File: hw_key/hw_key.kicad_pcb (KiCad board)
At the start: 2 copper layers, 127 x 38.1 mm, 30 parts, among them P2 CONN_01X10, SW1 SW_PUSH_SMALL_H, SW10 SW_PUSH_SMALL_H, SW11 SW_PUSH_SMALL_H, SW12 SW_PUSH_SMALL_H, SW2 SW_PUSH_SMALL_H, SW3 SW_PUSH_SMALL_H, SW4 SW_PUSH_SMALL_H, SW5 SW_PUSH_SMALL_H, SW6 SW_PUSH_SMALL_H, SW7 SW_PUSH_SMALL_H, SW8 SW_PUSH_SMALL_H, SW9 SW_PUSH_SMALL_H

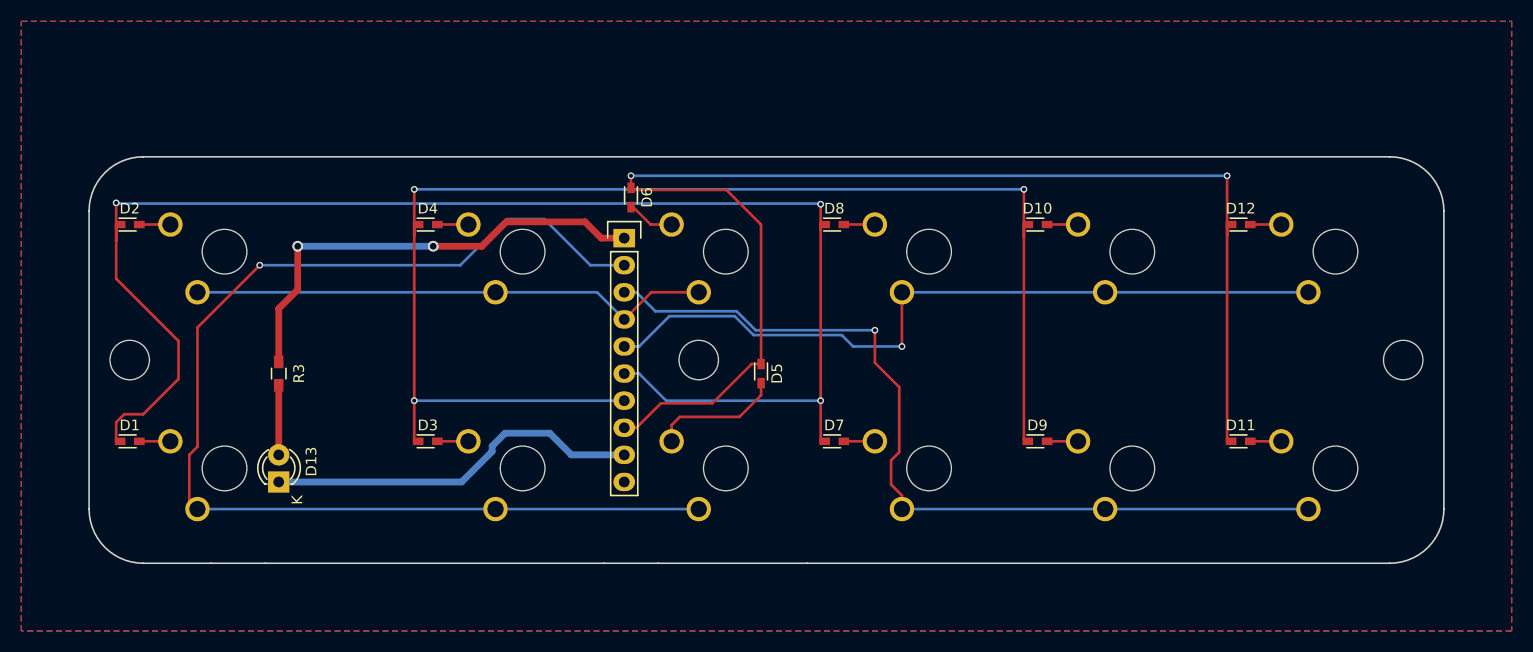
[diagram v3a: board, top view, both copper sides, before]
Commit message: hole position, corner rounding size
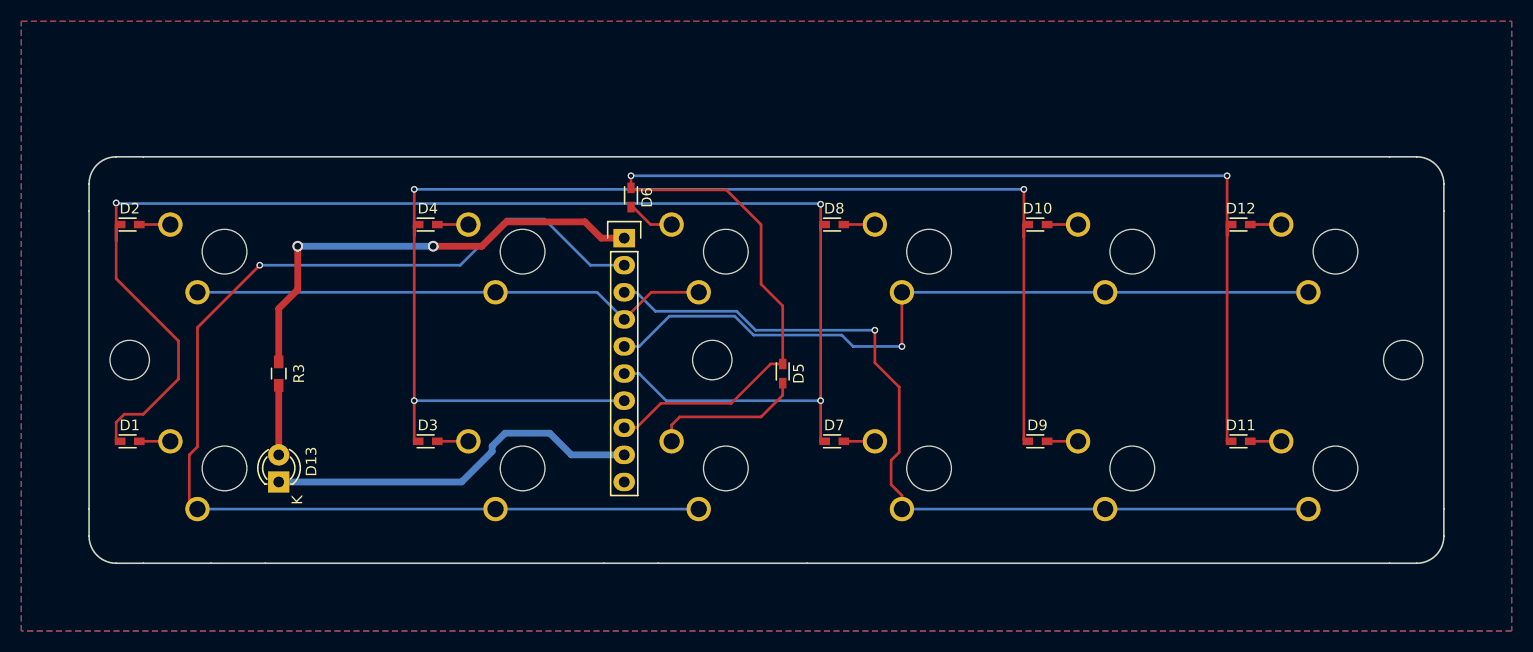
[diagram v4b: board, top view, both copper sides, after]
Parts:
- moved D5 2.03 mm to (90.4, 45.7)
- moved REF** 1.27 mm to (83.8, 44.5)
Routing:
- net /kR2: track 125.8 -> 128.6 mm
- net Net-(D5-Pad2): track 12.2 -> 14.2 mm
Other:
- outline, holes or cut-outs redrawn
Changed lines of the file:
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@@
     (area 19.05 12.7 158.750001 69.850001)
     (thickness 1.6)
-    (drawings 14)
-    (tracks 144)
+    (drawings 22)
+    (tracks 146)
     (zones 0)
     (modules 30)
@@
     (mod_text_size 1 1)
     (mod_text_width 0.15)
-    (pad_size 1.5 1.5)
-    (pad_drill 0.8)
+    (pad_size 3.7 3.7)
+    (pad_drill 3.7)
     (pad_to_mask_clearance 0.2)
     (aux_axis_origin 0 0)
@@
   )
   (module Mounting_Holes:MountingHole_3.7mm (layer F.Cu)
-    (at 82.55 44.45)
+    (at 83.82 44.45)
     (descr "Mounting Hole 3.7mm, no annular")
     (tags "mounting hole 3.7mm no annular")
@@
   )
   (module components:SOD-523-handsoldering (layer F.Cu)
-    (at 88.392 45.72 270)
+    (at 90.424 45.72 270)
     (descr "http://www.diodes.com/datasheets/ap02001.pdf p.144")
     (tags "Diode SOD523")
@@
     (pad 1 np_thru_hole circle (at 0 0) (size 3.7 3.7) (drill 3.7) (layers *.Cu *.Mask))
   )
+  (gr_line (start 25.4 60.96) (end 25.4 58.42) (angle 90) (layer Edge.Cuts) (width 0.15))
+  (gr_line (start 27.94 63.5) (end 30.48 63.5) (angle 90) (layer Edge.Cuts) (width 0.15))
+  (gr_line (start 25.4 27.94) (end 25.4 30.48) (angle 90) (layer Edge.Cuts) (width 0.15))
+  (gr_line (start 30.48 25.4) (end 27.94 25.4) (angle 90) (layer Edge.Cuts) (width 0.15))
+  (gr_line (start 149.86 63.5) (end 147.32 63.5) (angle 90) (layer Edge.Cuts) (width 0.15))
+  (gr_line (start 152.4 60.96) (end 152.4 58.42) (angle 90) (layer Edge.Cuts) (width 0.15))
+  (gr_line (start 152.4 27.94) (end 152.4 30.48) (angle 90) (layer Edge.Cuts) (width 0.15))
+  (gr_line (start 149.86 25.4) (end 147.32 25.4) (angle 90) (layer Edge.Cuts) (width 0.15))
+  (gr_arc (start 149.86 27.94) (end 149.86 25.4) (angle 90) (layer Edge.Cuts) (width 0.15))
+  (gr_arc (start 149.86 60.96) (end 152.4 60.96) (angle 90) (layer Edge.Cuts) (width 0.15))
+  (gr_arc (start 27.94 60.96) (end 27.94 63.5) (angle 90) (layer Edge.Cuts) (width 0.15))
+  (gr_arc (start 27.94 27.94) (end 25.4 27.94) (angle 90) (layer Edge.Cuts) (width 0.15))
   (gr_line (start 36.83 63.5) (end 41.91 63.5) (angle 90) (layer Edge.Cuts) (width 0.15))
   (gr_line (start 78.74 63.5) (end 73.66 63.5) (angle 90) (layer Edge.Cuts) (width 0.15))
@@
   (gr_line (start 25.4 30.48) (end 25.4 58.42) (angle 90) (layer Edge.Cuts) (width 0.15))
   (gr_line (start 147.32 25.4) (end 30.48 25.4) (angle 90) (layer Edge.Cuts) (width 0.15))
-  (gr_arc (start 147.32 30.48) (end 147.32 25.4) (angle 90) (layer Edge.Cuts) (width 0.15))
-  (gr_arc (start 147.32 58.42) (end 152.4 58.42) (angle 90) (layer Edge.Cuts) (width 0.15))
-  (gr_arc (start 30.48 58.42) (end 30.48 63.5) (angle 90) (layer Edge.Cuts) (width 0.15))
-  (gr_arc (start 30.48 30.48) (end 25.4 30.48) (angle 90) (layer Edge.Cuts) (width 0.15))
   (target plus (at 25.4 25.4) (size 5) (width 0.15) (layer Edge.Cuts))
   (segment (start 30.11 52.07) (end 33.02 52.07) (width 0.254) (layer F.Cu) (net 1) (status 30))
@@
   (segment (start 60.96 52.07) (end 58.05 52.07) (width 0.254) (layer F.Cu) (net 3) (status 30))
   (segment (start 60.96 31.75) (end 58.05 31.75) (width 0.254) (layer F.Cu) (net 4) (status 30))
-  (segment (start 88.392 46.62) (end 88.392 47.752) (width 0.254) (layer F.Cu) (net 5) (status 10))
+  (segment (start 90.424 46.62) (end 90.424 47.752) (width 0.254) (layer F.Cu) (net 5) (status 10))
+  (segment (start 88.392 49.784) (end 80.772 49.784) (width 0.254) (layer F.Cu) (net 5))
+  (segment (start 80.772 49.784) (end 80.01 50.546) (width 0.254) (layer F.Cu) (net 5))
   (segment (start 80.01 50.546) (end 80.01 52.07) (width 0.254) (layer F.Cu) (net 5) (status 20))
-  (segment (start 80.772 49.784) (end 80.01 50.546) (width 0.254) (layer F.Cu) (net 5))
-  (segment (start 86.36 49.784) (end 80.772 49.784) (width 0.254) (layer F.Cu) (net 5))
-  (segment (start 88.392 47.752) (end 86.36 49.784) (width 0.254) (layer F.Cu) (net 5))
+  (segment (start 90.424 47.752) (end 88.392 49.784) (width 0.254) (layer F.Cu) (net 5))
   (segment (start 80.01 31.75) (end 78.04 31.75) (width 0.254) (layer F.Cu) (net 6) (status 10))
   (segment (start 78.04 31.75) (end 76.2 29.91) (width 0.254) (layer F.Cu) (net 6) (status 20))
@@
   (segment (start 113.157 52.07) (end 113.4 52.07) (width 0.254) (layer F.Cu) (net 16) (status 30))
   (segment (start 55.88 48.26) (end 55.88 32.766) (width 0.254) (layer F.Cu) (net 16))
-  (segment (start 88.392 44.82) (end 87.514 44.82) (width 0.254) (layer F.Cu) (net 17) (status 10))
+  (segment (start 78.994 48.514) (end 85.598 48.514) (width 0.254) (layer F.Cu) (net 17))
+  (segment (start 89.292 44.82) (end 90.424 44.82) (width 0.254) (layer F.Cu) (net 17) (status 20))
+  (segment (start 85.598 48.514) (end 89.292 44.82) (width 0.254) (layer F.Cu) (net 17))
+  (segment (start 90.424 44.82) (end 90.424 39.37) (width 0.254) (layer F.Cu) (net 17) (status 10))
+  (segment (start 88.392 31.75) (end 85.152 28.51) (width 0.254) (layer F.Cu) (net 17))
+  (segment (start 85.152 28.51) (end 76.2 28.51) (width 0.254) (layer F.Cu) (net 17) (status 20))
+  (segment (start 88.392 31.75) (end 88.392 37.338) (width 0.254) (layer F.Cu) (net 17))
+  (segment (start 90.424 39.37) (end 88.392 37.338) (width 0.254) (layer F.Cu) (net 17))
   (segment (start 76.708 50.8) (end 75.565 50.8) (width 0.254) (layer F.Cu) (net 17) (status 20))
   (segment (start 78.994 48.514) (end 76.708 50.8) (width 0.254) (layer F.Cu) (net 17))
-  (segment (start 83.82 48.514) (end 78.994 48.514) (width 0.254) (layer F.Cu) (net 17))
-  (segment (start 87.514 44.82) (end 83.82 48.514) (width 0.254) (layer F.Cu) (net 17))
-  (segment (start 88.392 31.75) (end 88.392 44.82) (width 0.254) (layer F.Cu) (net 17) (status 20))
   (segment (start 132.08 52.07) (end 132.08 32.766) (width 0.254) (layer F.Cu) (net 17) (status 10))
   (segment (start 132.08 52.07) (end 132.45 52.07) (width 0.254) (layer F.Cu) (net 17) (status 30))
@@
   (segment (start 76.2 28.51) (end 76.2 27.178) (width 0.254) (layer F.Cu) (net 17) (status 10))
   (via (at 132.08 27.178) (size 0.635) (drill 0.381) (layers F.Cu B.Cu) (net 17))
-  (segment (start 85.152 28.51) (end 76.2 28.51) (width 0.254) (layer F.Cu) (net 17) (status 20))
-  (segment (start 88.392 31.75) (end 85.152 28.51) (width 0.254) (layer F.Cu) (net 17))
   (segment (start 68.58 51.308) (end 64.389 51.308) (width 0.635) (layer B.Cu) (net 18))
   (segment (start 70.612 53.34) (end 68.58 51.308) (width 0.635) (layer B.Cu) (net 18))

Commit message: revamp boards (for assembled height)
flip logic over so that it can mate closely with key; reset button moves
to same side as all the other parts; board assembly down to ~16mm high
and assembly more easily lends itself to angling for even less height at
the front for slightly more in the back
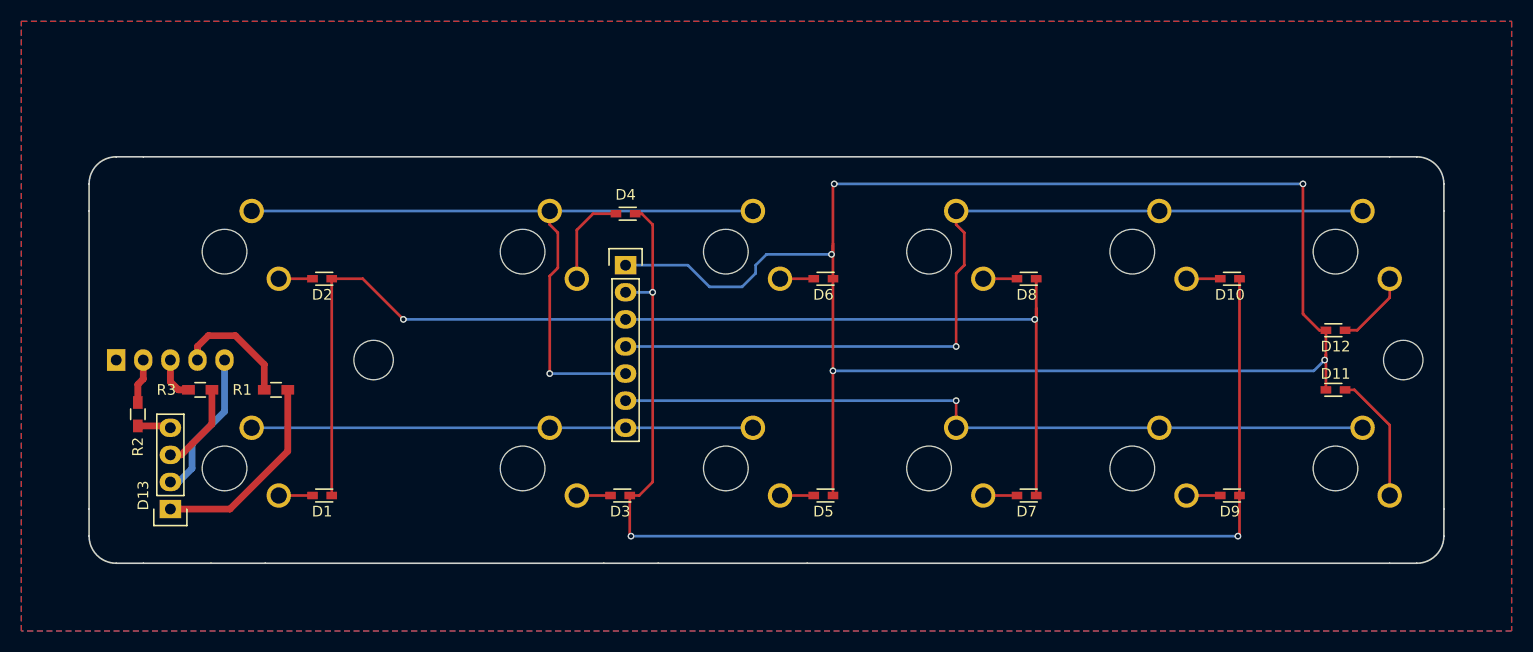
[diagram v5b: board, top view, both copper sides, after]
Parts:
- removed the REF** at (29.2, 44.5)
- added P1: CONN_01X07, Pin_Headers:Pin_Header_Straight_1x07, F.Cu at (75.7, 35.6)
- added R1: 330, Resistors_SMD:R_0603_HandSoldering, F.Cu at (42.9, 47.2)
- added R2: 330, Resistors_SMD:R_0603_HandSoldering, F.Cu at (30.0, 49.5)
- D13: value LED -> LED_RABG; footprint LEDs:LED-3MM -> Pin_Headers:Pin_Header_Straight_1x04
- P2: value CONN_01X10 -> CONN_01X05; footprint Pin_Headers:Pin_Header_Straight_1x10 -> Pin_Headers:Pin_Header_Straight_1x05; moved to B.Cu
- moved P2 49.0 mm to (27.9, 44.5), turned to 270 degrees
- moved REF** 31.7 mm to (52.1, 44.5)
- moved D6 19.6 mm to (94.2, 36.8), turned to 180 degrees
- moved D10 18.7 mm to (132.3, 36.8), turned to 180 degrees
- moved D7 18.7 mm to (113.3, 57.1), turned to 180 degrees
- moved D8 18.7 mm to (113.3, 36.8), turned to 180 degrees
- moved D9 18.7 mm to (132.3, 57.1), turned to 180 degrees
- moved D1 18.7 mm to (47.2, 57.1), turned to 180 degrees
- moved D2 18.7 mm to (47.2, 36.8), turned to 180 degrees
- moved D3 18.7 mm to (75.2, 57.1), turned to 180 degrees
- moved D4 18.6 mm to (75.7, 30.7), turned to 180 degrees
- moved D12 13.3 mm to (142.2, 41.7)
- moved D5 12.0 mm to (94.2, 57.1), turned to 180 degrees
- moved D13 10.5 mm to (33.0, 58.4), turned to 180 degrees
- moved D11 10.1 mm to (142.2, 47.2)
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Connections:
- D13 pad 1: /kLED_MACRO -> Net-(D13-Pad1)
- D13 pad 2: Net-(D13-Pad2) -> +3V3
- P2 pad 1: +3V3 -> GND
- P2 pad 2: /kC0 -> /LED_B
- P2 pad 3: /kC1 -> /LED_G
- P2 pad 4: /kC2 -> /LED_R
- P2 pad 5: /kC3 -> +3V3
- R3 pad 1: +3V3 -> Net-(D13-Pad3)
- R3 pad 2: Net-(D13-Pad2) -> /LED_G
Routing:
- net /kC0: track 110.6 -> 47.0 mm, vias 1 -> 0
- net /kLED_MACRO: track 35.4 -> 0.00 mm
- net /kR2: track 128.6 -> 163.6 mm, vias 2 -> 5
- net /kR0: track 140.1 -> 109.3 mm, vias 3 -> 2
- net +3V3: track 43.8 -> 14.0 mm, vias 2 -> 0
- net /kC2: track 49.1 -> 70.0 mm, vias 0 -> 1
- net Net-(D13-Pad1): track 0.00 -> 19.0 mm
- net /LED_R: track 0.00 -> 11.4 mm
- net /kR1: track 127.6 -> 116.3 mm
- net Net-(D5-Pad2): track 14.2 -> 3.16 mm
- net /kC3: track 71.6 -> 82.4 mm
- net /kC1: track 81.5 -> 71.6 mm
- net Net-(D11-Pad2): track 2.91 -> 12.2 mm
- net Net-(D13-Pad3): track 0.00 -> 8.30 mm
- net Net-(D13-Pad2): track 6.52 -> 0.00 mm
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
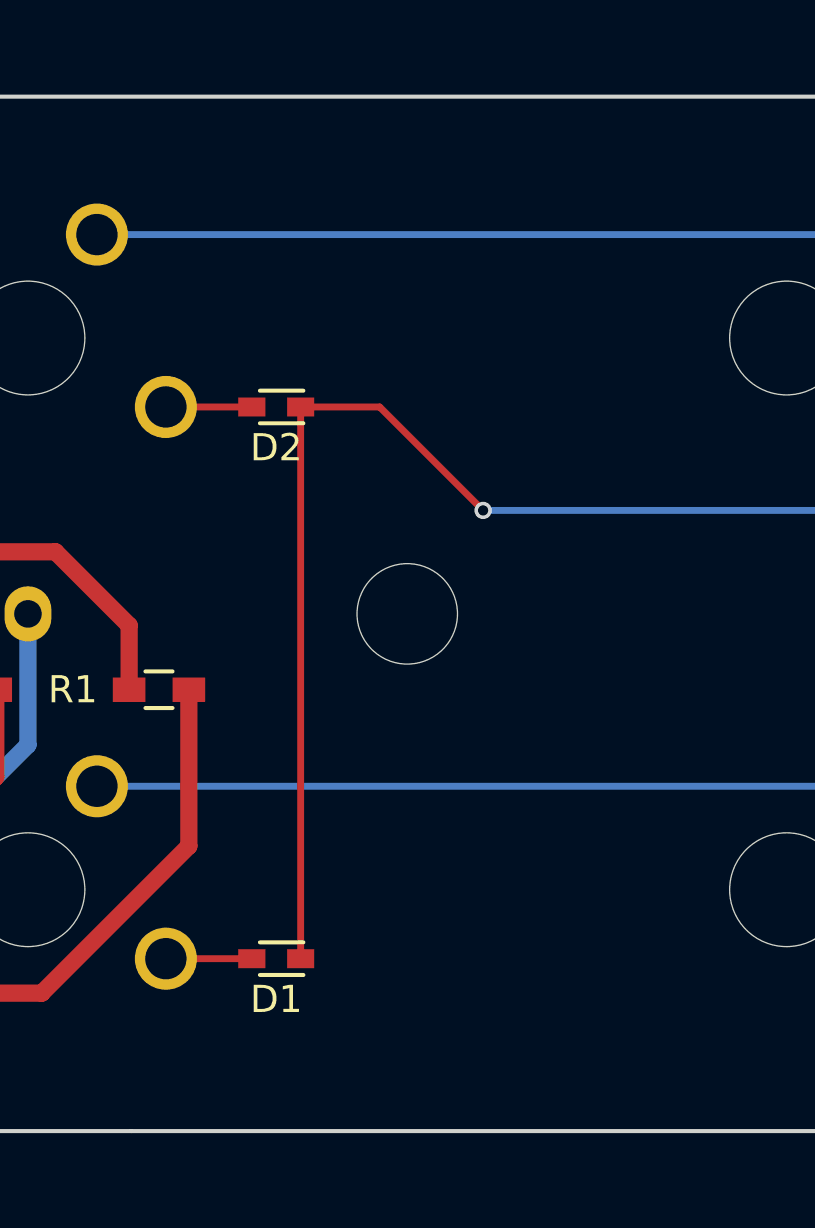
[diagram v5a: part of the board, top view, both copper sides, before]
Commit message: final PCB revisions
plus the start of a case to hold them
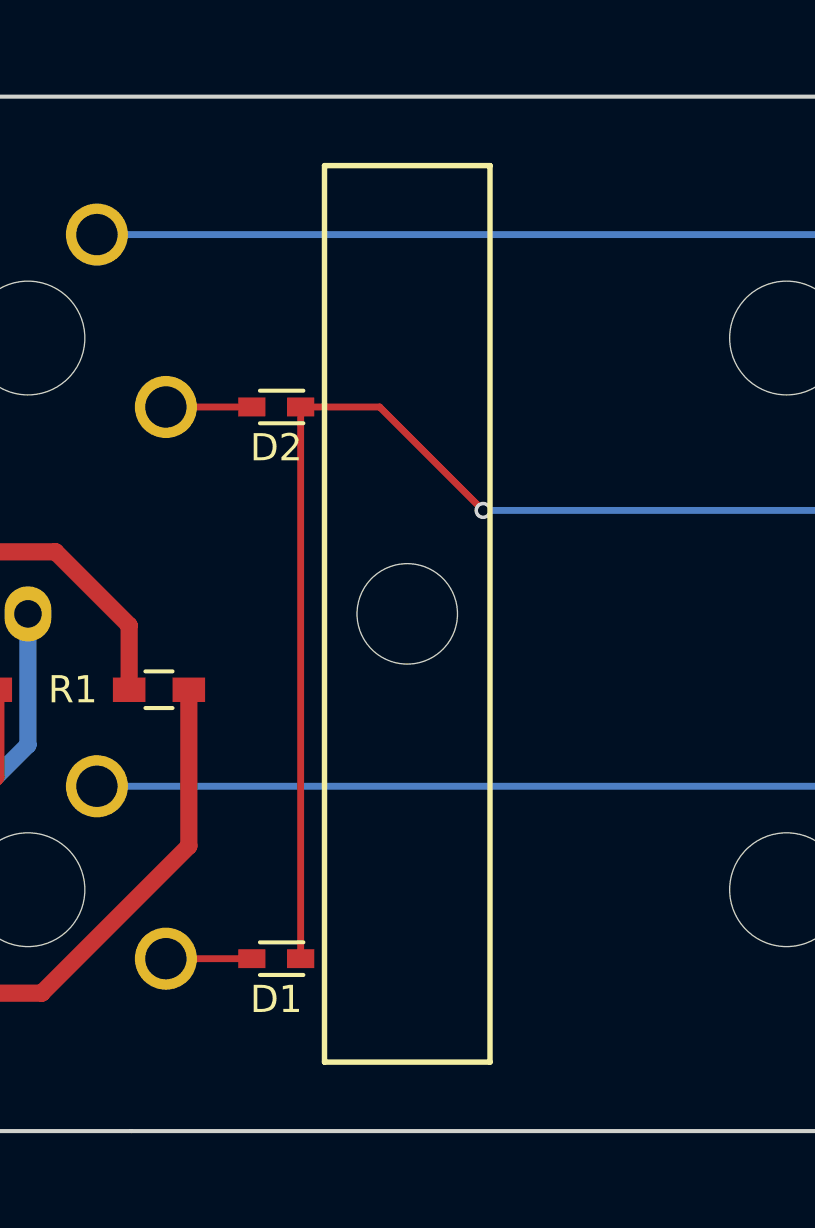
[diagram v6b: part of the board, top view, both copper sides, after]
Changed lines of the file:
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@@
     (area 19.05 12.7 158.750001 69.850001)
     (thickness 1.6)
-    (drawings 22)
+    (drawings 26)
     (tracks 125)
     (zones 0)
@@
     )
   )
+  (gr_line (start 55.118 27.94) (end 49.022 27.94) (angle 90) (layer F.SilkS) (width 0.2))
+  (gr_line (start 55.118 60.96) (end 55.118 27.94) (angle 90) (layer F.SilkS) (width 0.2))
+  (gr_line (start 55.118 60.96) (end 49.022 60.96) (angle 90) (layer F.SilkS) (width 0.2))
+  (gr_line (start 49.022 27.94) (end 49.022 60.96) (angle 90) (layer F.SilkS) (width 0.2))
   (gr_line (start 25.4 60.96) (end 25.4 58.42) (angle 90) (layer Edge.Cuts) (width 0.15))
   (gr_line (start 27.94 63.5) (end 30.48 63.5) (angle 90) (layer Edge.Cuts) (width 0.15))
@@
   (segment (start 38.1 49.276) (end 35.052 52.324) (width 0.635) (layer B.Cu) (net 13))
   (segment (start 33.782 55.88) (end 33.02 55.88) (width 0.635) (layer B.Cu) (net 13))
-  (segment (start 75.692 38.1) (end 78.232 38.1) (width 0.254) (layer B.Cu) (net 15) (status 400000))
+  (segment (start 75.692 38.1) (end 78.232 38.1) (width 0.254) (layer B.Cu) (net 15))
   (via (at 78.232 38.1) (size 0.635) (drill 0.381) (layers F.Cu B.Cu) (net 15))
   (segment (start 133.234 57.15) (end 133.234 60.822) (width 0.254) (layer F.Cu) (net 15))
@@
   (segment (start 33.782 47.244) (end 33.02 46.482) (width 0.635) (layer F.Cu) (net 26))
   (segment (start 35.56 44.45) (end 35.56 43.18) (width 0.635) (layer F.Cu) (net 27))
-  (segment (start 41.826 44.874) (end 41.826 47.244) (width 0.635) (layer F.Cu) (net 27) (status 800000))
+  (segment (start 41.826 44.874) (end 41.826 47.244) (width 0.635) (layer F.Cu) (net 27))
   (segment (start 39.116 42.164) (end 41.826 44.874) (width 0.635) (layer F.Cu) (net 27))
   (segment (start 36.576 42.164) (end 39.116 42.164) (width 0.635) (layer F.Cu) (net 27))
